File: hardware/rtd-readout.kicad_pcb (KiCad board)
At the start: 4 copper layers, 122 x 104 mm, 51 parts, among them J1 Conn_RTD_4W, J2 Conn_RTD_4W, J3 Conn_RTD_4W, J4 Conn_T7_Analog, J5 Conn_T7_I2C, J6 Conn_Power, J7 Conn_RTD_4W, U1 ADS1115IDGS (0x48), U2 ADS1115IDGS (0x49)

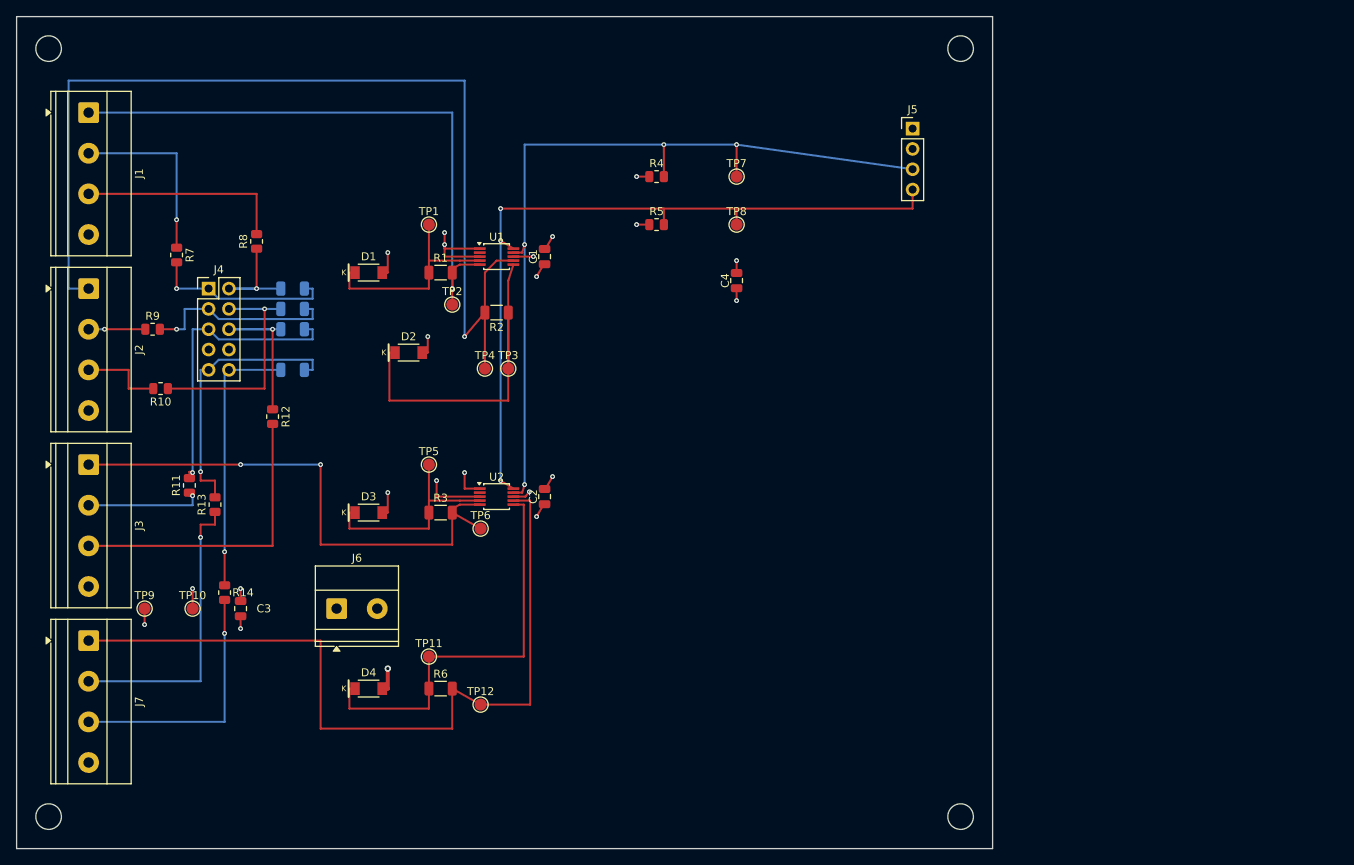
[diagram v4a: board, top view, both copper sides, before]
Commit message: rev-G: enclosure integration - 100x159.5 board, Hammond 1455N, RJ45/PT/KK I/O
Board resized to slide into a Hammond 1455N1601 extrusion (machinable end
panels, connectors proud/flush through cutouts). All parts live-verified
with adversarial fact-checks:
- RTD inputs: 4x Phoenix PT 1,5/5-3,5-H push-in blocks (pin 5 = cable
  shield to AGND); kept terminal blocks over RJ45 for bare cryo cables.
- T7 analog: Amphenol RJHSE-5380 shielded RA RJ45, T568 pair mapping
  (CH1=1/2, CH2=3/6, CH3=4/5, CH4=7/8), shield+chassis bond at the jack.
- T7 I2C: Molex KK 254 friction-lock header; pin numbers reversed (1<->4,
  2<->3) to make the fan planar - pigtail map in PANELS_AND_PINOUTS.md.
- Routing: via-free corridor (y 63-81) carries the 4 sense pairs to a C0G
  cap ladder + gated T568 fan; I2C as parallel diagonals; +5V south edge.
- Deliverables: docs/PANELS_AND_PINOUTS.md, panel machining DXFs, renders.

Gates: ERC 0/0, DRC 0 violations / 0 unconnected, SPICE 7/7 PASS.
DRC iteration trail: 92 -> 32 -> 8 -> 1 -> 0.

Co-Authored-By: Claude Fable 5 <noreply@anthropic.com>
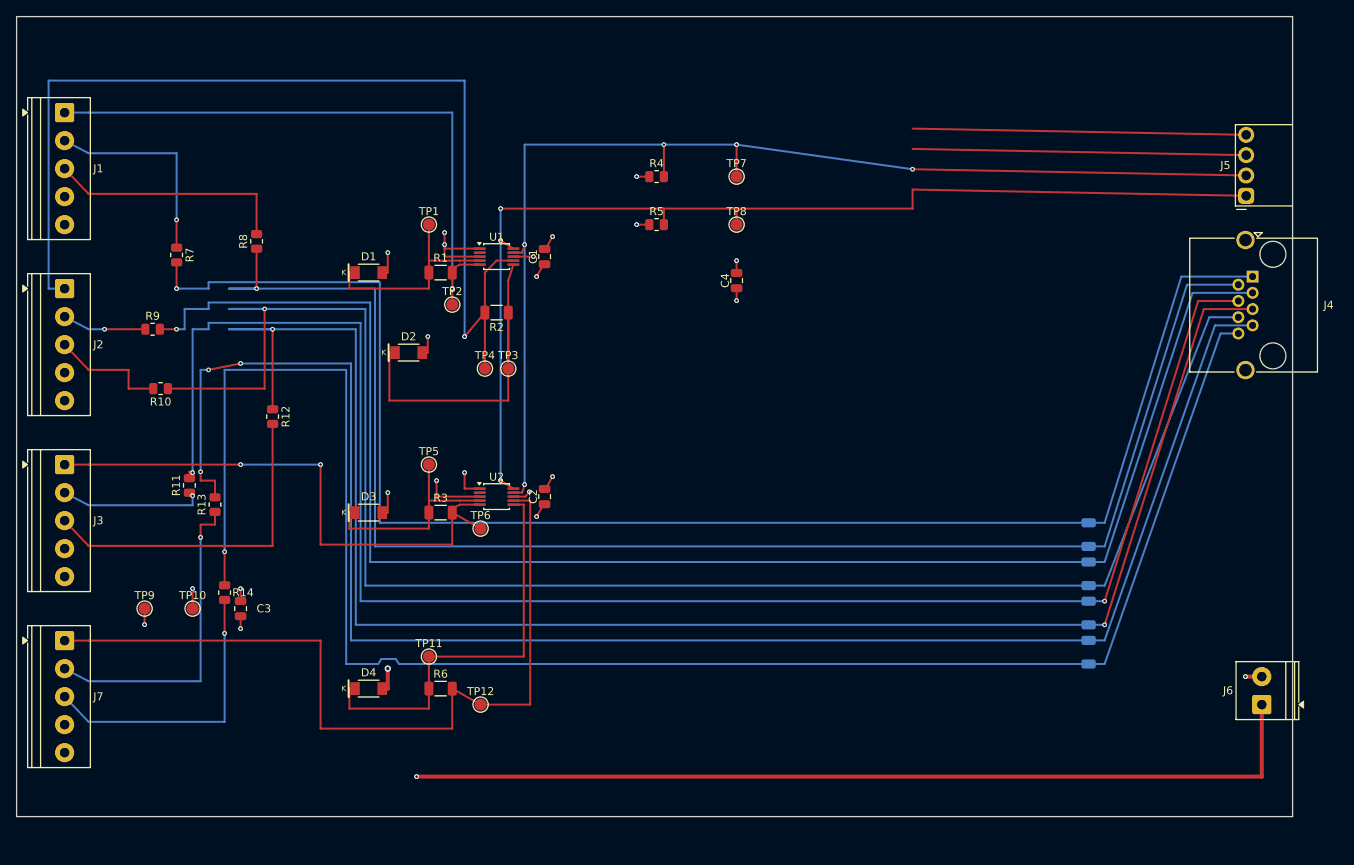
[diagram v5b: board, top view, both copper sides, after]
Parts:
- removed ? (x4): , 
- J1, J2, J3: footprint rtd-readout:TerminalBlock_Phoenix_MKDS-1,5-4-5.08_1x04_P5.08mm_Horizontal -> rtd-readout:TerminalBlock_Phoenix_PT-1,5-5-3.5-H_1x05_P3.50mm_Horizontal
- J4: value Conn_T7_Analog -> Conn_T7_RJ45; footprint PinHeader_2x05_P2.54mm_Vertical -> rtd-readout:RJ45_Amphenol_RJHSE5380
- J5: footprint rtd-readout:PinHeader_1x04_P2.54mm_Vertical -> rtd-readout:Molex_KK-254_AE-7395-04A_1x04_P2.54mm_Horizontal
- J6: footprint rtd-readout:TerminalBlock_Phoenix_MKDS-1,5-2-5.08_1x02_P5.08mm_Horizontal -> rtd-readout:TerminalBlock_Phoenix_PT-1,5-2-3.5-H_1x02_P3.50mm_Horizontal
- J7: footprint TerminalBlock_Phoenix_MKDS-1,5-4-5.08_1x04_P5.08mm_Horizontal -> rtd-readout:TerminalBlock_Phoenix_PT-1,5-5-3.5-H_1x05_P3.50mm_Horizontal
- moved J4 130.5 mm to (154.5, 32.5), turned to -90 degrees
- moved J6 116.3 mm to (155.7, 86.0), turned to 90 degrees
- moved C7 105.6 mm to (134.0, 74.5), turned to 90 degrees
- moved C8 105.6 mm to (134.0, 79.5), turned to 90 degrees
- moved C6 104.9 mm to (134.0, 69.7), turned to 90 degrees
- moved C5 104.1 mm to (134.0, 64.8), turned to 90 degrees
- moved J5 42.5 mm to (153.7, 22.4), turned to 90 degrees
- moved J1 3.00 mm to (6.00, 12.0)
- moved J2 3.00 mm to (6.00, 34.0)
- moved J3 3.00 mm to (6.00, 56.0)
- moved J7 3.00 mm to (6.00, 78.0)
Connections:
- J4 pad 4: CH2_T7- -> CH3_T7+
- J4 pad 5: CH3_T7+ -> CH3_T7-
- J4 pad 6: CH3_T7- -> CH2_T7-
- J4 pad 7: GND -> CH4_T7+
- J4 pad 8: GND -> CH4_T7-
- J5 pad 1: VS -> SCL
- J5 pad 2: GND -> SDA
- J5 pad 3: SDA -> GND
- J5 pad 4: SCL -> VS
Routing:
- net CH3_T7-: track 21.9 -> 209.3 mm, vias 1 -> 2
- net CH4_T7-: track 33.9 -> 220.3 mm
- net CH4_T7+: track 34.6 -> 211.9 mm, vias 1 -> 3
- net CH2_T7-: track 33.0 -> 210.1 mm
- net CH3_T7+: track 37.0 -> 213.1 mm, vias 1 -> 2
- net CH1_T7-: track 14.9 -> 190.8 mm
- net CH2_T7+: track 24.0 -> 196.3 mm
- net CH1_T7+: track 23.1 -> 191.3 mm
- net +5V: track 16.0 -> 130.7 mm, vias 6 -> 7
- net GND: track 32.6 -> 76.4 mm, vias 8 -> 9
- net SDA: track 103.5 -> 145.2 mm, vias 4 -> 5
- net VS: track 17.6 -> 59.3 mm
- net SCL: track 95.7 -> 137.4 mm
- net CH1_SENSE-: track 26.0 -> 30.3 mm
- net CH2_SENSE-: track 10.4 -> 14.7 mm
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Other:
- board size 122 x 104 mm -> 159.5 x 100 mm

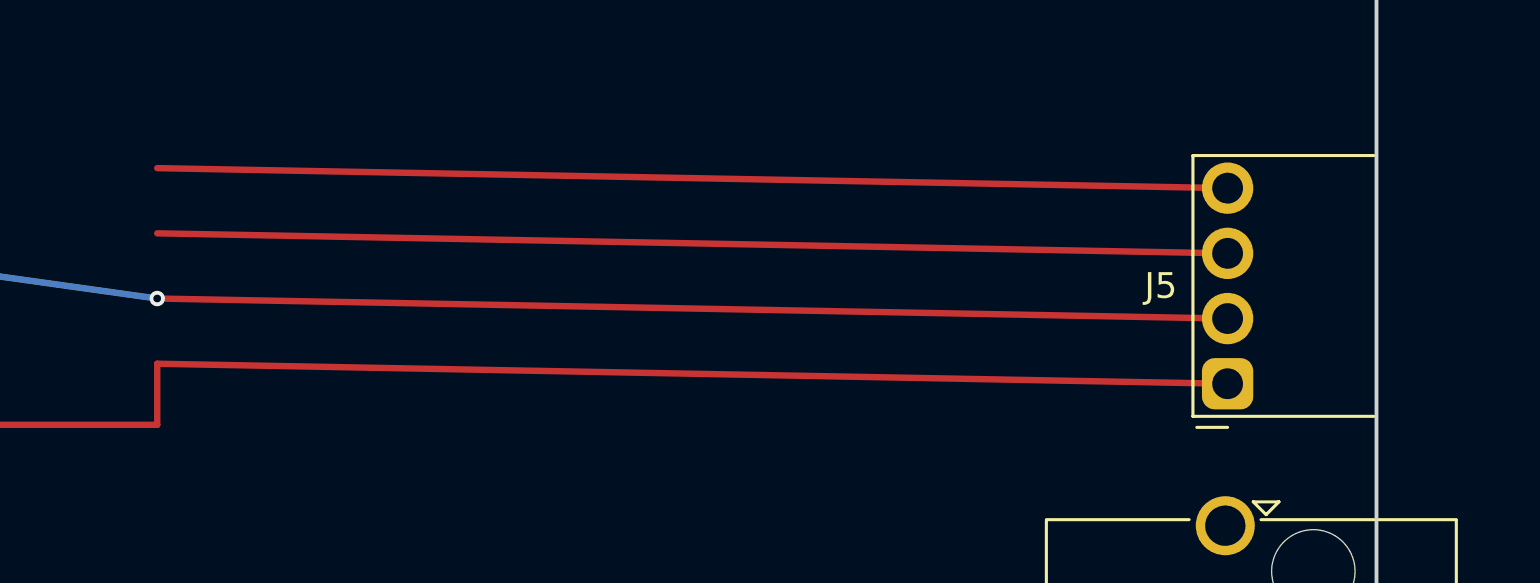
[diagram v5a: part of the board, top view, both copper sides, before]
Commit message: rev-G.1: J5 -> Molex PicoBlade 53048-0410 (no-crimp pre-made pigtail 2181120404)
Lucas found the 218112 PicoBlade pigtail family - swapped the I2C header
so the pre-made 425mm assembly plugs straight in (zero crimping). Pin
order (1=SCL..4=VS) unchanged; I2C re-routed as 4 parallel diagonals to
the new 1.25mm pads. Panel DXF, PANELS_AND_PINOUTS, BOM_REVIEW, order
CSV updated; DKRed zip regenerated.

Gates: ERC 0/0, DRC 0 violations / 0 unconnected.

Co-Authored-By: Claude Fable 5 <noreply@anthropic.com>
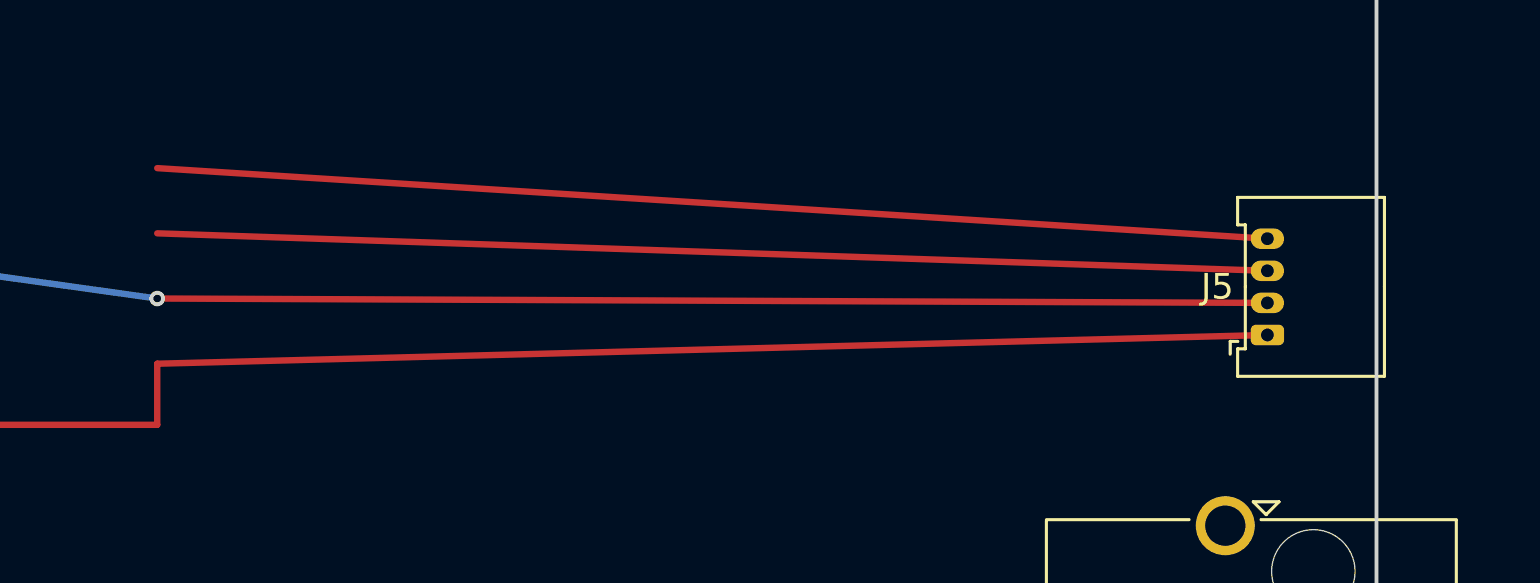
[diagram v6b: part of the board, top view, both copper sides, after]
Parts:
- J5: footprint rtd-readout:Molex_KK-254_AE-7395-04A_1x04_P2.54mm_Horizontal -> rtd-readout:Molex_PicoBlade_53048-0410_1x04_P1.25mm_Horizontal
- moved J5 2.45 mm to (155.2, 20.5)
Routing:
- net VS: track 59.3 -> 60.9 mm
- net GND: track 76.4 -> 78.0 mm
- net SCL: track 137.4 -> 138.9 mm
- net SDA: track 145.2 -> 146.8 mm
